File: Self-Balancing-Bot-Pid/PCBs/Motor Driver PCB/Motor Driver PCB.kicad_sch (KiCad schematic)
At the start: 2 parts, among them IC1 AS5600-ASOT, U1 A4988SETTR-T

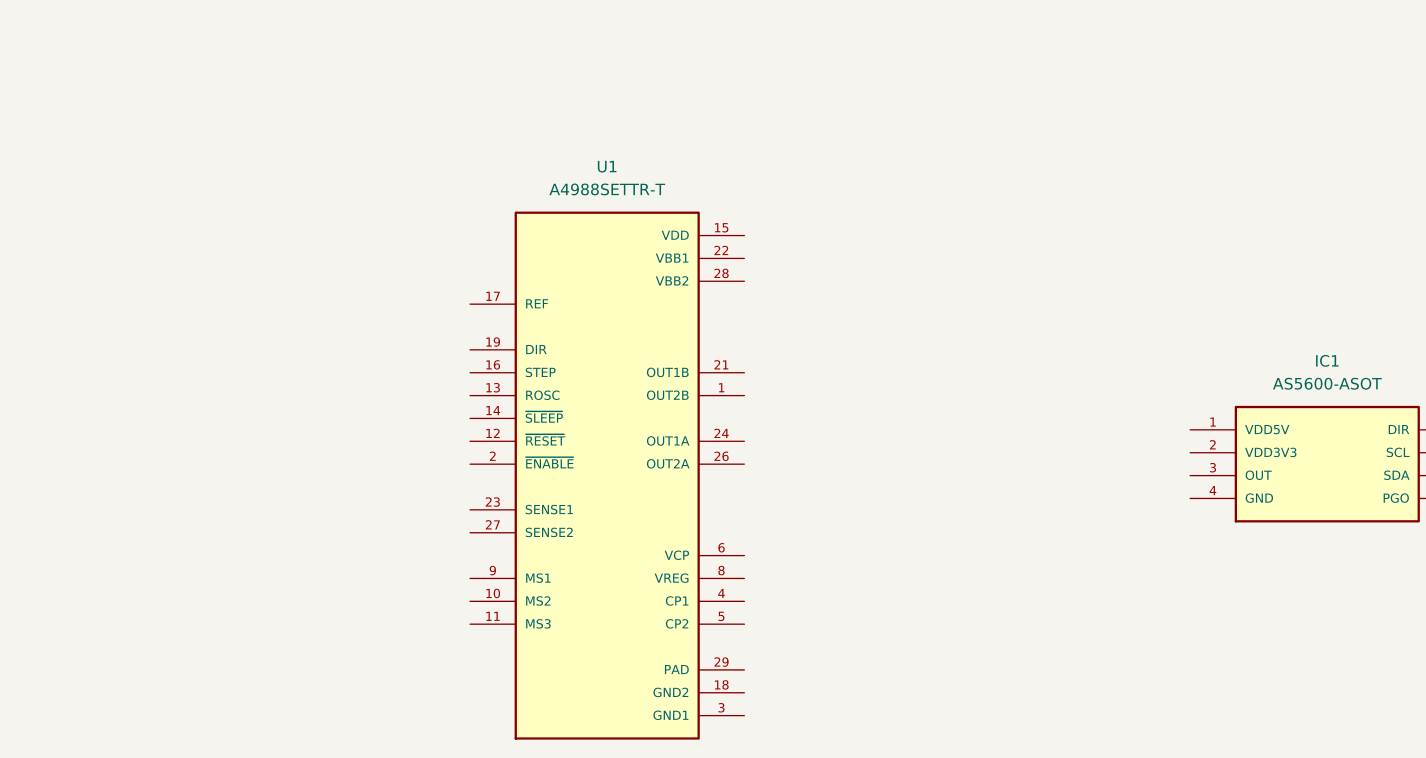
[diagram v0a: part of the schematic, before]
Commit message: Edited footprint of key components. Need to fix git ignore for auto gen files
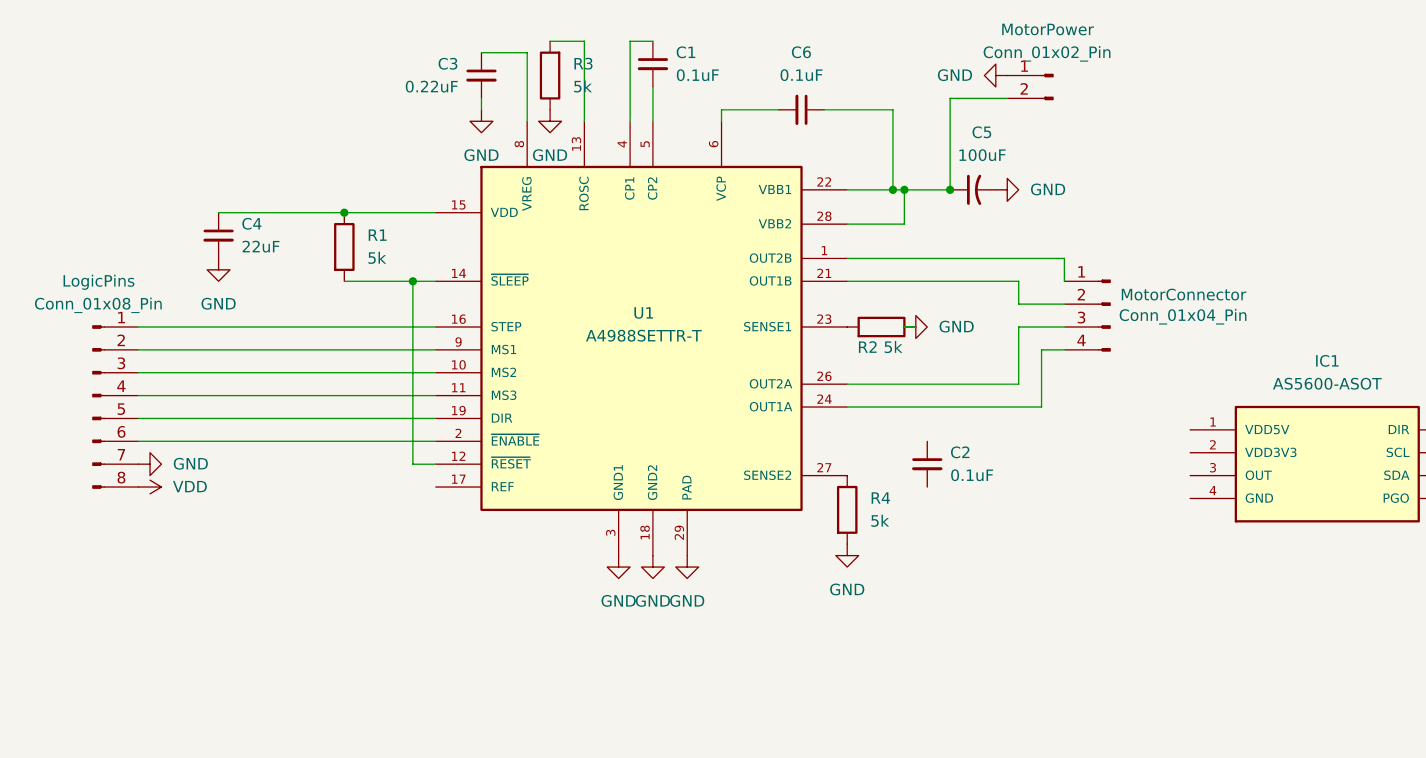
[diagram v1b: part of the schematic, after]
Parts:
- added C1, C2, C6: 0.1uF, Capacitor_SMD:C_0603_1608Metric, symbol Device:C_Small
- added C3: 0.22uF, Capacitor_SMD:C_0603_1608Metric, symbol Device:C_Small
- added C4: 22uF, Capacitor_SMD:C_0603_1608Metric, symbol Device:C_Small
- added C5: 100uF, Capacitor_SMD:C_0603_1608Metric, symbol Device:C_Small_US
- added LogicPins: Conn_01x08_Pin, Connector_PinHeader_2.54mm:PinHeader_1x08_P2.54mm_Horizontal, symbol Connector:Conn_01x08_Pin
- added MotorConnector: Conn_01x04_Pin, Connector_PinHeader_2.54mm:PinHeader_1x04_P2.54mm_Horizontal, symbol Connector:Conn_01x04_Pin
- added MotorPower: Conn_01x02_Pin, Connector_PinHeader_2.54mm:PinHeader_1x02_P2.54mm_Horizontal, symbol Connector:Conn_01x02_Pin
- added R1, R2, R3, R4: 5k, Capacitor_SMD:C_0603_1608Metric, symbol Device:R
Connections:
- net at U1.1 (OUT2B): now also MotorConnector.1 (Pin_1)
- net at U1.10 (MS2): now also LogicPins.3 (Pin_3)
- net at U1.11 (MS3): now also LogicPins.4 (Pin_4)
- net at U1.12 (~{RESET}): now also U1.14 (~{SLEEP}), R1.2
- net at U1.13 (ROSC): now also R3.2
- net at U1.15 (VDD): now also C4.1, R1.1
- net at U1.16 (STEP): now also LogicPins.1 (Pin_1)
- net GND: now reaches U1.18 (GND2)
- net GND: now also U1.29 (PAD), U1.3 (GND1), C3.2, C4.2, C5.2, LogicPins.7 (Pin_7), MotorPower.1 (Pin_1), R2.1, R3.1, R4.2
- net at U1.19 (DIR): now also LogicPins.5 (Pin_5)
- net at U1.2 (~{ENABLE}): now also LogicPins.6 (Pin_6)
- net at U1.21 (OUT1B): now also MotorConnector.2 (Pin_2)
- net at U1.22 (VBB1): now also U1.28 (VBB2), C5.1, C6.1, MotorPower.2 (Pin_2)
- net at U1.23 (SENSE1): now also R2.2
- net at U1.24 (OUT1A): now also MotorConnector.4 (Pin_4)
- net at U1.26 (OUT2A): now also MotorConnector.3 (Pin_3)
- net at U1.27 (SENSE2): now also R4.1
- net at U1.4 (CP1): now also C1.1
- net at U1.5 (CP2): now also C1.2
- net at U1.6 (VCP): now also C6.2
- net at U1.8 (VREG): now also C3.1
- net at U1.9 (MS1): now also LogicPins.2 (Pin_2)
- new net VDD: LogicPins.8 (Pin_8)
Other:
- moved on the sheet: U1

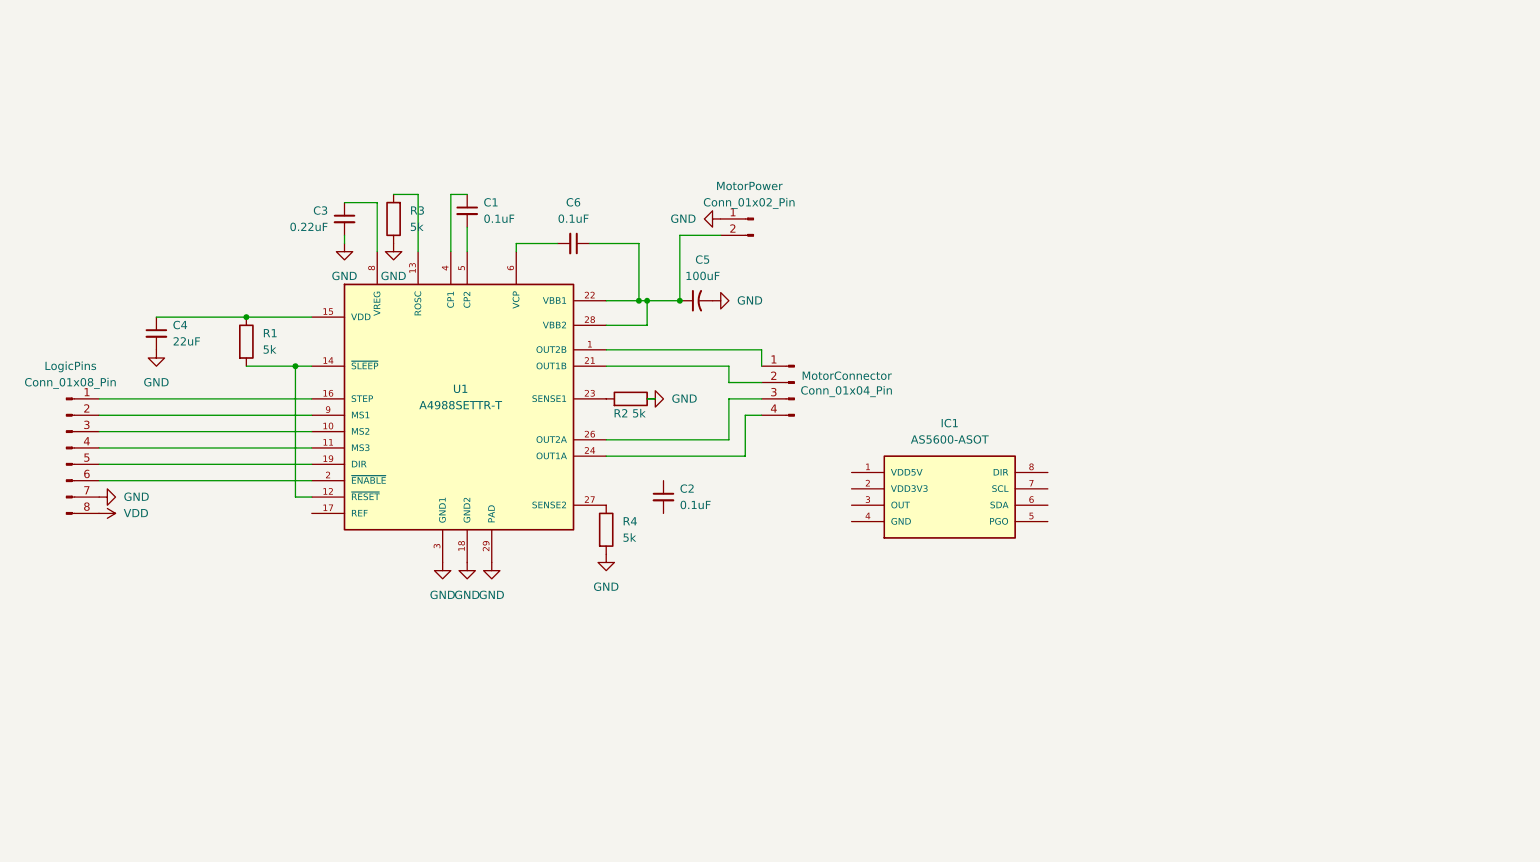
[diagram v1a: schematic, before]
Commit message: Completed a4988 IC integration
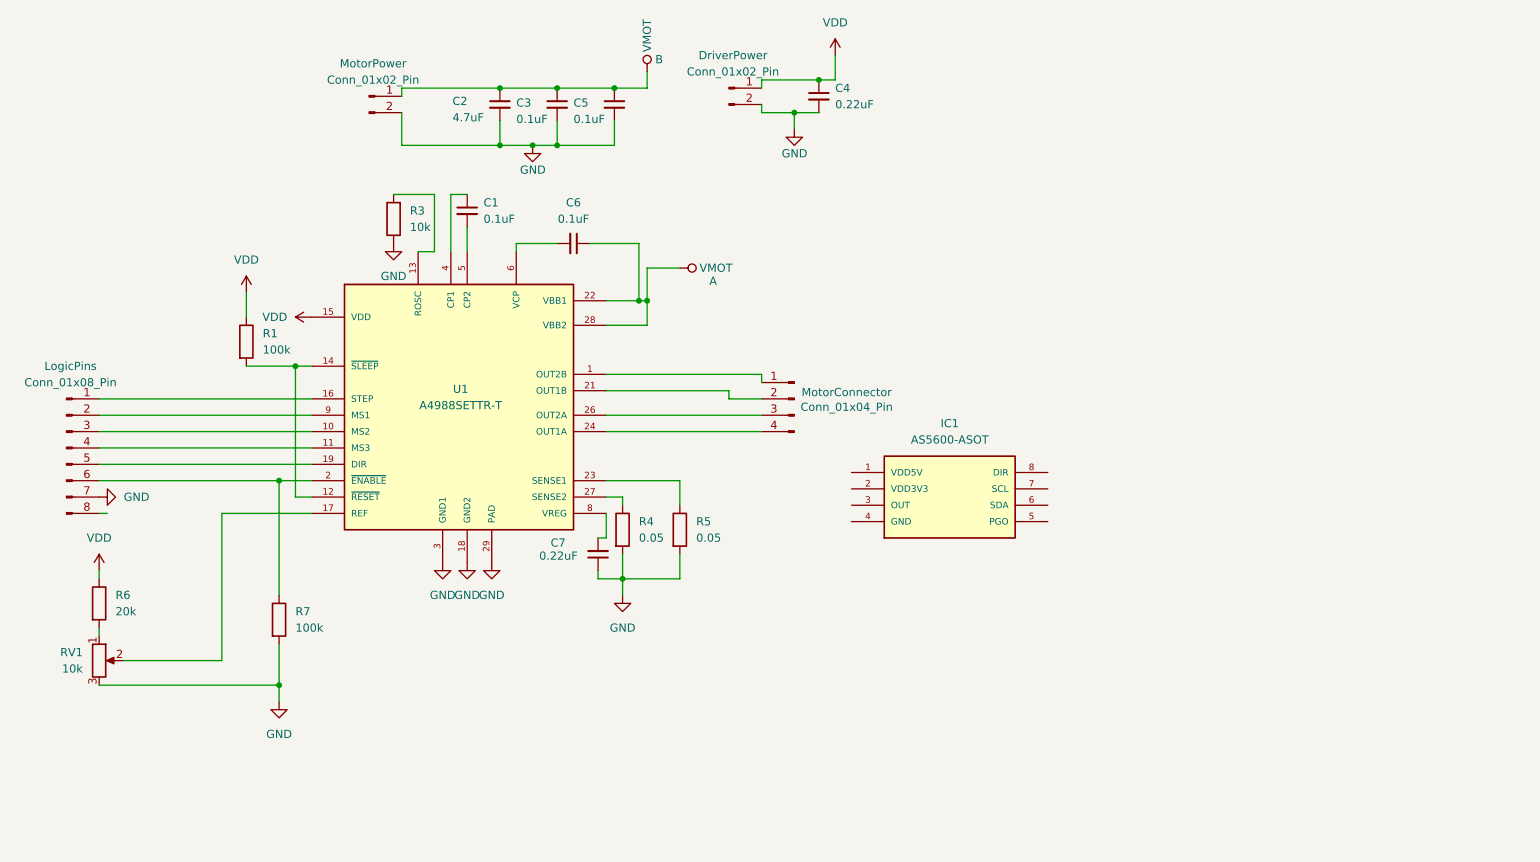
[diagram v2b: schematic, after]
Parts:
- removed C5: 100uF, Capacitor_SMD:C_0603_1608Metric, symbol Device:C_Small_US
- removed R2: 5k, Capacitor_SMD:C_0603_1608Metric, symbol Device:R
- added A, B: ~, symbol VMOT:VMOT
- added C5: 0.1uF, Capacitor_SMD:C_0603_1608Metric, symbol Device:C_Small
- added C7: 0.22uF, Capacitor_SMD:C_0603_1608Metric, symbol Device:C_Small
- added DriverPower: Conn_01x02_Pin, Connector_JST:JST_PH_B2B-PH-K_1x02_P2.00mm_Vertical, symbol Connector:Conn_01x02_Pin
- added R5: 0.05, Resistor_SMD:R_0603_1608Metric, symbol Device:R
- added R6: 20k, Resistor_SMD:R_0603_1608Metric, symbol Device:R
- added R7: 100k, Resistor_SMD:R_0603_1608Metric, symbol Device:R
- added RV1: 10k, Potentiometer_SMD:Potentiometer_Bourns_3269W_Vertical, symbol Device:R_Potentiometer
- C2: value 0.1uF -> 4.7uF
- C3: value 0.22uF -> 0.1uF
- C4: value 22uF -> 0.22uF
- MotorConnector: footprint Connector_PinHeader_2.54mm:PinHeader_1x04_P2.54mm_Horizontal -> Connector_JST:JST_PH_B4B-PH-K_1x04_P2.00mm_Vertical
- MotorPower: footprint Connector_PinHeader_2.54mm:PinHeader_1x02_P2.54mm_Horizontal -> Connector_JST:JST_PH_B2B-PH-K_1x02_P2.00mm_Vertical
- R1: value 5k -> 100k; footprint Capacitor_SMD:C_0603_1608Metric -> Resistor_SMD:R_0603_1608Metric
- R3: value 5k -> 10k; footprint Capacitor_SMD:C_0603_1608Metric -> Resistor_SMD:R_0603_1608Metric
- R4: value 5k -> 0.05; footprint Capacitor_SMD:C_0603_1608Metric -> Resistor_SMD:R_0603_1608Metric
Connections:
- net GND: now also C2.2, MotorPower.2 (Pin_2), C5.2, C7.1, DriverPower.2 (Pin_2), R5.2, R7.2, RV1.3; no longer MotorPower.1 (Pin_1)
- net VDD: now also C4.1, R1.1, U1.15 (VDD), DriverPower.1 (Pin_1), R6.1; no longer LogicPins.8 (Pin_8)
- net at C6.1, U1.22 (VBB1), U1.28 (VBB2): now also A. (VMOT); no longer MotorPower.2 (Pin_2)
- net at C2.1: now also C3.1, MotorPower.1 (Pin_1), B. (VMOT), C5.1
- net at U1.8 (VREG): now also C7.2; no longer C3.1
- net at LogicPins.6 (Pin_6), U1.2 (~{ENABLE}): now also R7.1
- net at U1.23 (SENSE1): now also R5.1
- net at U1.17 (REF): now also RV1.2
- new net: R6.2, RV1.1
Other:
- moved on the sheet: MotorConnector, R4

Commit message: Completed schematic, now working on pcb
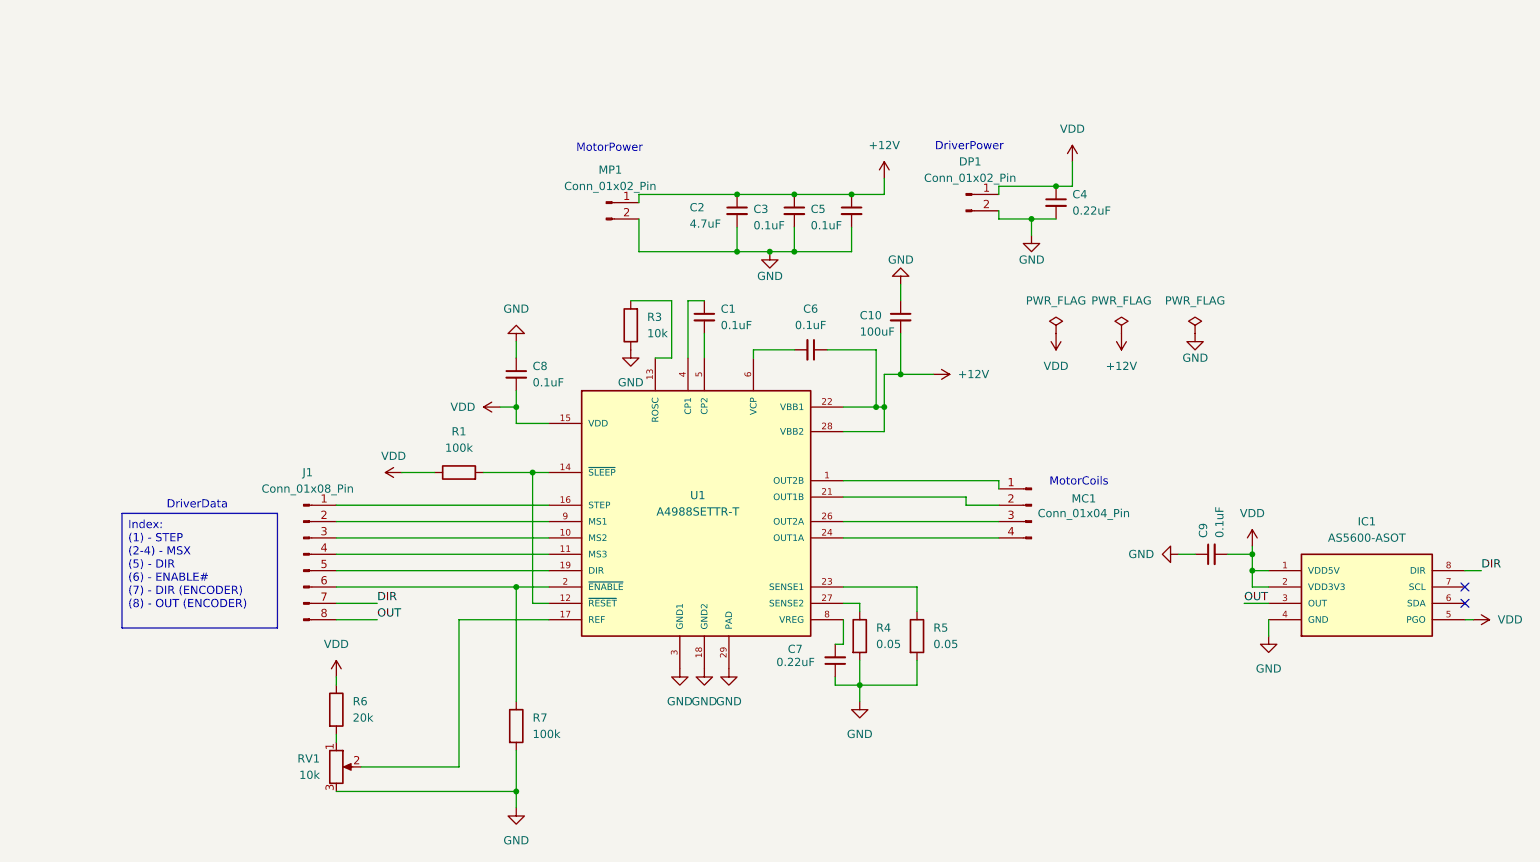
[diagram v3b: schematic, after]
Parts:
- removed A, B: ~, symbol VMOT:VMOT
- removed LogicPins: Conn_01x08_Pin, Connector_PinHeader_2.54mm:PinHeader_1x08_P2.54mm_Horizontal, symbol Connector:Conn_01x08_Pin
- added C10: 100uF, Capacitor_SMD:C_0603_1608Metric, symbol Device:C_Small
- added C8, C9: 0.1uF, Capacitor_SMD:C_0603_1608Metric, symbol Device:C_Small
- added J1: Conn_01x08_Pin, Connector_JST:JST_PH_B8B-PH-K_1x08_P2.00mm_Vertical, symbol Connector:Conn_01x08_Pin
- renumbered DriverPower to DP1, MotorConnector to MC1, MotorPower to MP1
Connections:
- net GND: now also IC1.4 (GND), C10.1, C8.1, C9.1
- net VDD: now also IC1.1 (VDD5V), IC1.2 (VDD3V3), IC1.5 (PGO), C8.2, C9.2
- net +12V: now reaches C2.1, C3.1, C5.1, MP1.1 (Pin_1)
- net +12V: now also C6.1, U1.22 (VBB1), U1.28 (VBB2), C10.2
- net OUT: now reaches IC1.3 (OUT)
- net OUT: now also J1.8 (Pin_8)
- net DIR: now reaches IC1.8 (DIR)
- net DIR: now also J1.7 (Pin_7)
- net at U1.16 (STEP): now also J1.1 (Pin_1)
- net at U1.9 (MS1): now also J1.2 (Pin_2)
- net at U1.10 (MS2): now also J1.3 (Pin_3)
- net at U1.11 (MS3): now also J1.4 (Pin_4)
- net at U1.19 (DIR): now also J1.5 (Pin_5)
- net at R7.1, U1.2 (~{ENABLE}): now also J1.6 (Pin_6)
- no-connect marks 0 -> 2
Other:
- note added: "DriverData"
- note added: "DriverPower"
- note added: "MotorCoils"
- note added: "MotorPower"
- moved on the sheet: C1, C2, C3, C4, C5, C6, C7, DP1, IC1, MC1, MP1, R1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
